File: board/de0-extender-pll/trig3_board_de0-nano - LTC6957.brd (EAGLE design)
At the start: 160 x 75 mm, 94 parts, among them IC1 FT230XQ, J12 4p-2.54, J13 BU-SMB-V, J17 2p-2.54, J23 2p-2.54, J24 2p-2.54, J32 2p-2.54, J34 2p-2.54, J38 2p-2.54, J42 2p-2.54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

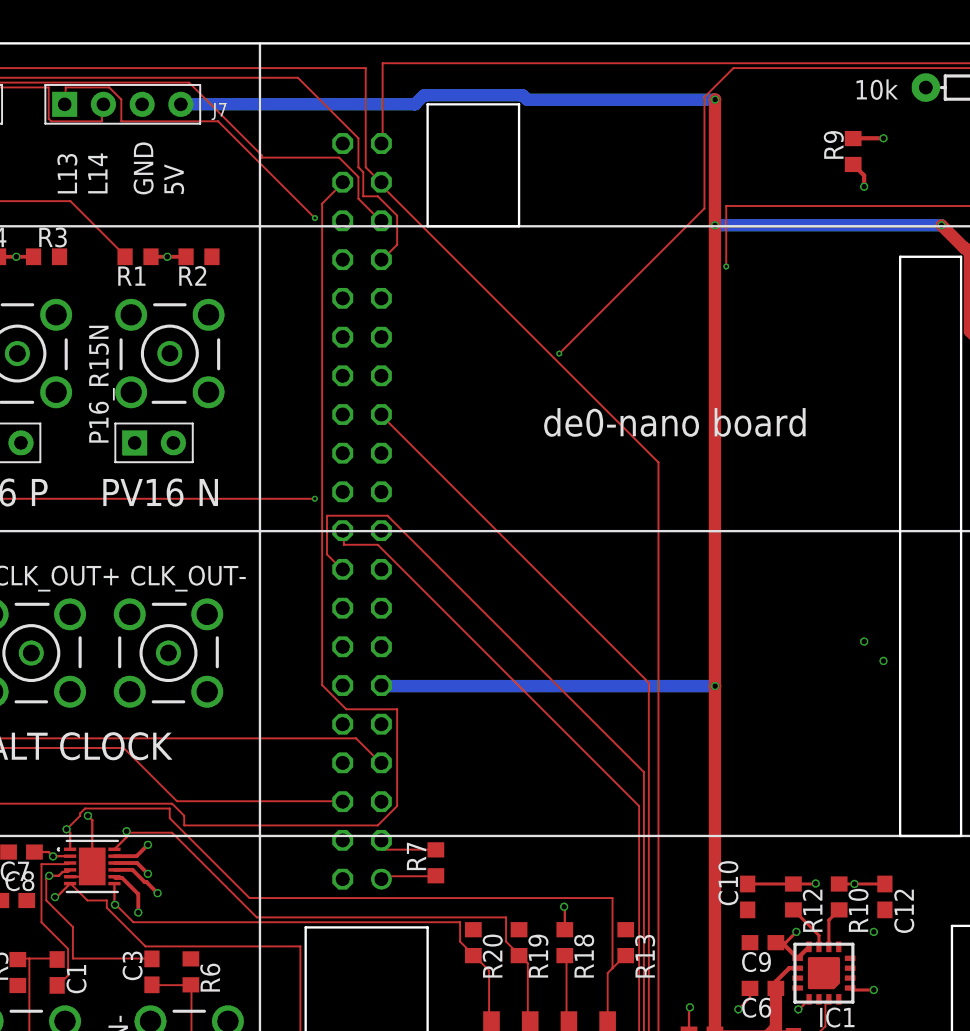
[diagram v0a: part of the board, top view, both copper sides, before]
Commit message: Update trig3_board_de0-nano - LTC6957.brd
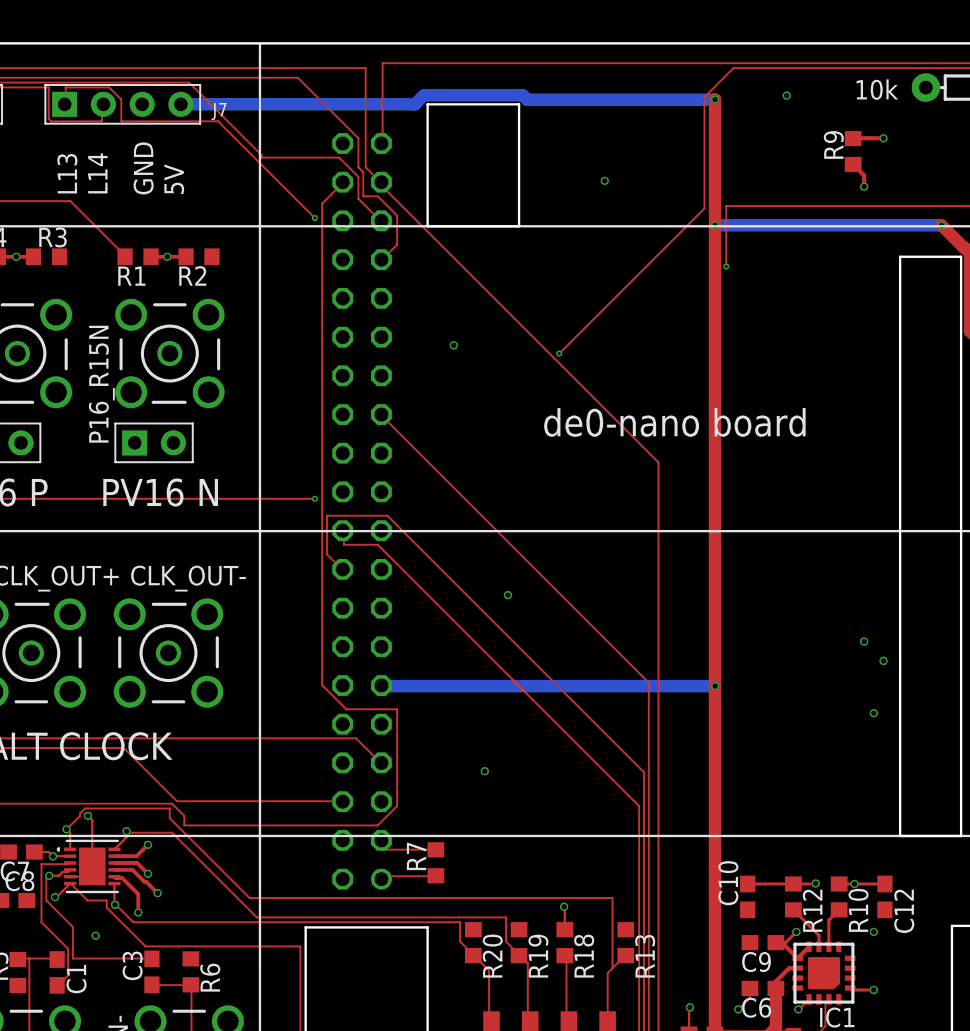
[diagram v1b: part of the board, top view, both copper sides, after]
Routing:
- net GND: vias 9 -> 10
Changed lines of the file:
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@@
 <wire x1="29.15" y1="47.692" x2="29.21" y2="47.752" width="0.1524" layer="1"/>
 <via x="29.21" y="47.752" extent="1-16" drill="0.35"/>
+<via x="23.622" y="101.981" extent="1-16" drill="0.35"/>
 </signal>
 <signal name="5V" class="1">
@@
 <wire x1="14.9225" y1="51.27625" x2="15" y2="51.15" width="0.127" layer="1"/>
 </signal>
+<signal name="GND1" airwireshidden="yes">
+<via x="13.716" y="91.186" extent="1-16" drill="0.35"/>
+</signal>
+<signal name="GND2" airwireshidden="yes">
+<via x="35.56" y="107.569" extent="1-16" drill="0.35"/>
+</signal>
+<signal name="GND3" airwireshidden="yes">
+<via x="17.272" y="74.803" extent="1-16" drill="0.35"/>
+</signal>
+<signal name="GND4" airwireshidden="yes">
+<via x="15.748" y="63.246" extent="1-16" drill="0.35"/>
+</signal>
+<signal name="GND6" airwireshidden="yes">
+<via x="41.275" y="67.056" extent="1-16" drill="0.35"/>
+</signal>
+<signal name="GND9" airwireshidden="yes">
+<via x="-9.779" y="52.451" extent="1-16" drill="0.35"/>
+</signal>
 </signals>

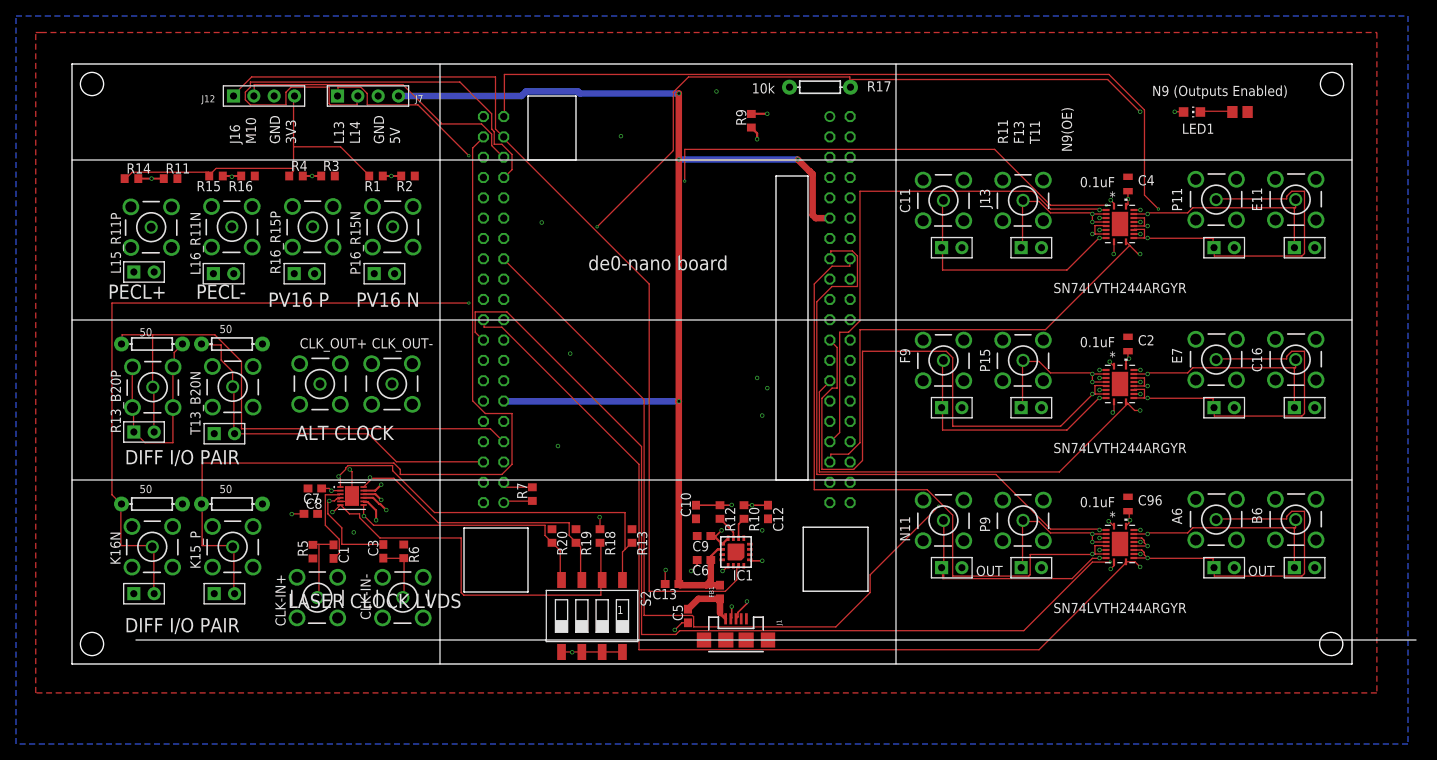
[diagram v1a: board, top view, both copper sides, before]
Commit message: fixed auto-router top layer nonsense
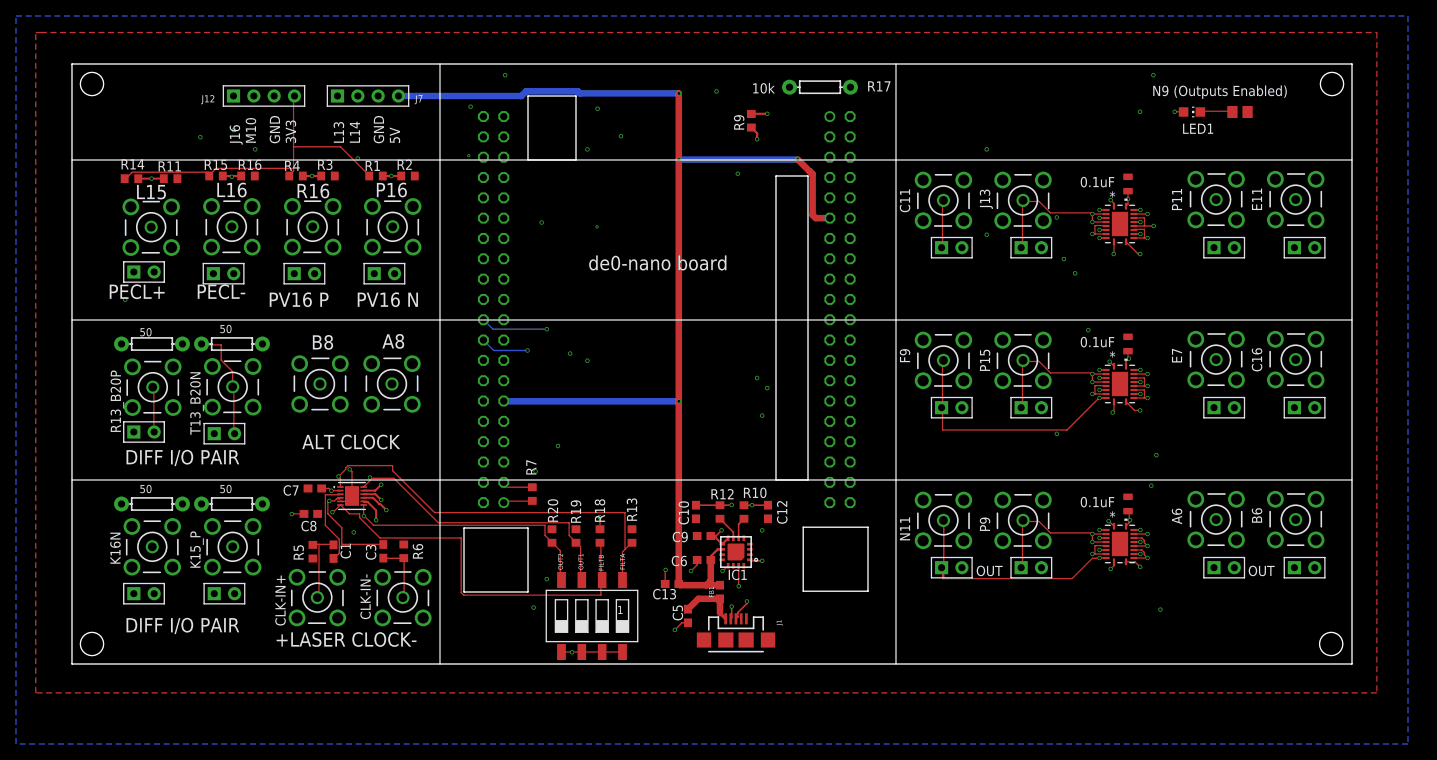
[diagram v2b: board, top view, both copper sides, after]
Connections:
- net N$15 renamed FILTA
- net N$16 renamed FILTB
- net N$17 renamed SD1
- net N$18 renamed SD2
- removed net N$1: J17.1, R13_B20P.2, R13_B20P.3, R13_B20P.4, R13_B20P.5, R161.P$1
- net GND: now also J17.1, R13_B20P.2, R13_B20P.3, R13_B20P.4, R13_B20P.5, R161.P$1
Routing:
- net GPIO_126_L14: track 63.7 -> 27.0 mm, vias 0 -> 1
- net GPIO_018_E7: track 80.5 -> 45.5 mm, vias 1 -> 2
- net N$1: track 26.5 -> 0.00 mm
- net OUT30: track 45.5 -> 19.1 mm
- net OUT38: track 45.5 -> 19.2 mm
- net OUT22: track 45.4 -> 19.0 mm
- net GPIO_110_P11: track 100.1 -> 115.0 mm, vias 3 -> 5
- net GPIO_14_R13: track 71.6 -> 57.9 mm
- net GPIO_022_F9: track 59.2 -> 45.6 mm
- net GPIO_011_A6: track 82.6 -> 69.4 mm, vias 1 -> 2
- net GPIO_131_K15: track 106.1 -> 95.0 mm, vias 0 -> 1
- net GPIO_120_P15: track 134.0 -> 123.0 mm, vias 2 -> 3
- net GPIO_028_C11: track 63.3 -> 72.9 mm, vias 2 -> 3
- net GPIO_010_B6: track 77.0 -> 67.7 mm, vias 2 -> 3
- net GPIO_130_J16: track 119.5 -> 123.8 mm, vias 0 -> 3
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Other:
- board text added: "+LASER CLOCK-"
- board text added: "A8"
- board text added: "B8"
- board text added: "FILTA"
- board text added: "FILTB"
- board text added: "L15"
- board text added: "L16"
- board text added: "OUT1"
- board text added: "OUT2"
- board text added: "P16"
- board text added: "R16"
- board text removed: "F13"
- board text removed: "LASER CLOCK LVDS"
- board text removed: "N9(OE)"
- board text removed: "R11"
- board text removed: "T11"

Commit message: removed wire stubs, tried to fix package rotation
rotated footprints in library but change did not propagate to pcb
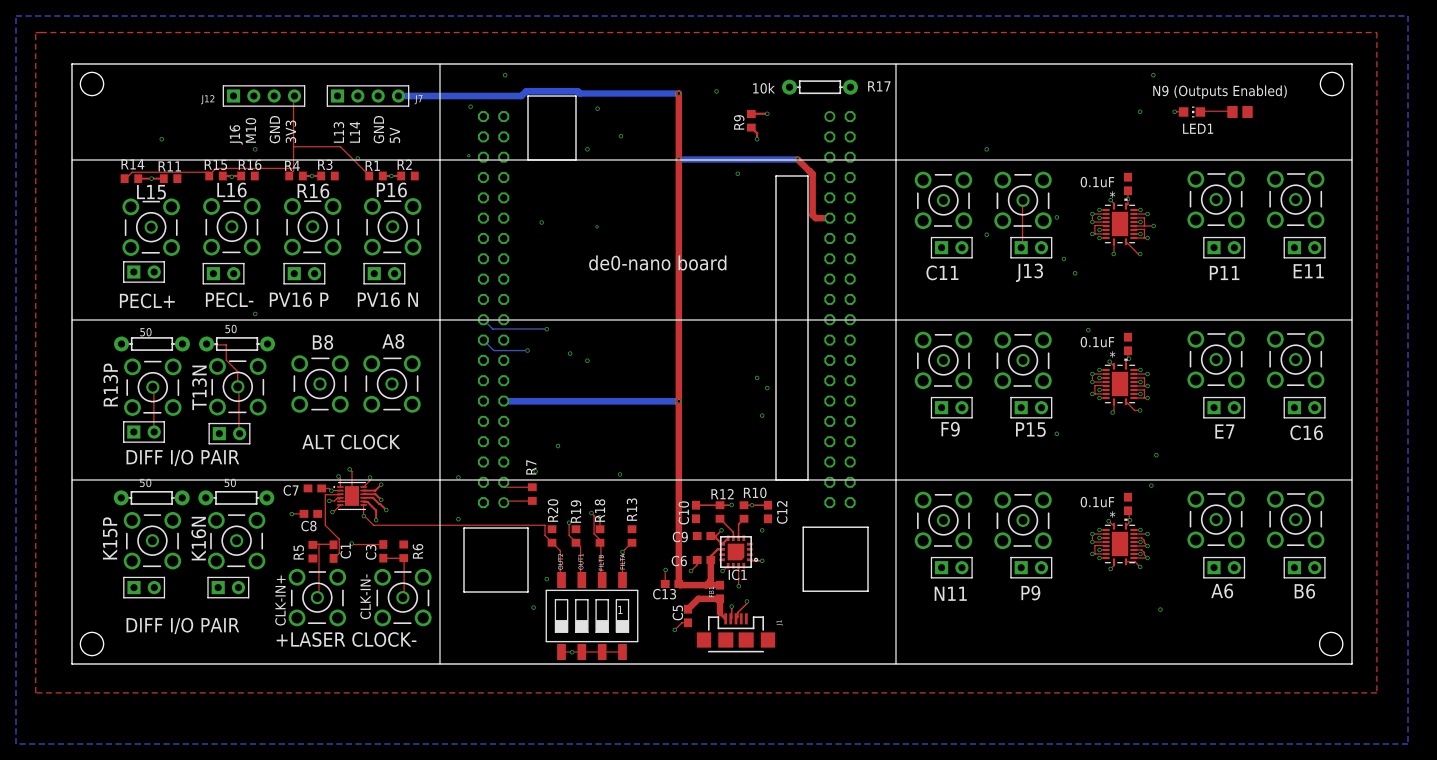
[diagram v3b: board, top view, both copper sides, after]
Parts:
- removed K15_P, T13_B20N: BU-SMB-V, con-coax:BU-SMB-V
- added K15P, T13N: BU-SMB-V, con-coax:BU-SMB-V
- C2, C4, C96: device SparkFun-Capacitors:0805 -> rcl:C0603
- R11, R16, R2, R3: value 83 -> 82
- moved K16N 10.6 mm to (-24.4, 51.4)
- moved R22 10.6 mm to (-24.5, 56.8)
- moved J23 10.6 mm to (-25.5, 45.6)
- moved J24 10.1 mm to (-36.0, 45.6)
- moved R23 10.1 mm to (-35.0, 56.8)
- moved J38 0.64 mm to (-25.3, 64.8)
- moved R32 0.64 mm to (-24.4, 76.0)
- renumbered R13_B20P to R13P
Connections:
- net GND: now also K15P.2, K15P.3, K15P.4, K15P.5, T13N.2, T13N.3, T13N.4, T13N.5; no longer K15_P.2, K15_P.3, K15_P.4, K15_P.5, T13_B20N.2, T13_B20N.3, T13_B20N.4, T13_B20N.5
- net GPIO_131_K15: now also K15P.1; no longer K15_P.1
- net GPIO_13_T13: now also T13N.1; no longer T13_B20N.1
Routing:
- net GPIO_117_K16: track 84.4 -> 71.8 mm
- net GPIO_131_K15: track 95.0 -> 103.2 mm
- net FILTB: track 49.7 -> 42.9 mm, vias 1 -> 2
- net OUT32: track 32.9 -> 29.2 mm
- net OUT24: track 32.1 -> 29.0 mm
- net SD1: track 36.7 -> 39.7 mm, vias 1 -> 4
- net FILTA: track 50.5 -> 52.4 mm, vias 1 -> 3
- net GPIO_13_T13: track 46.9 -> 46.3 mm
- net N$5: track 13.0 -> 12.3 mm, vias 1 -> 2
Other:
- board text removed: "OUT"

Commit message: rotated footprints and cosmetic updates to board
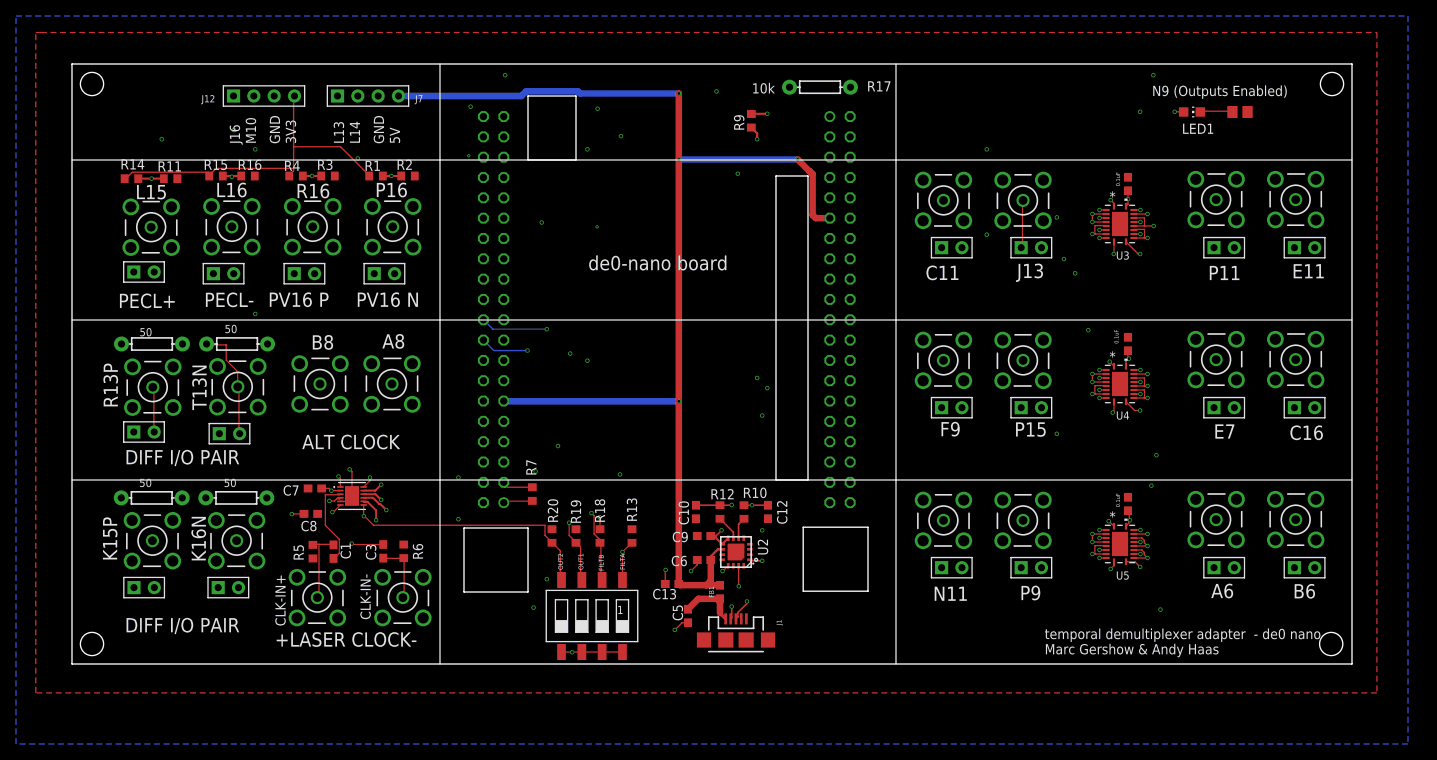
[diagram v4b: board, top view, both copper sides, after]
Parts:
- removed IC1: FT230XQ, ftdichip:QFN16
- added U2: FT230XQ, ftdichip-rotate-footprint-jlcpcb:QFN16
- turned U1 to 270 degrees
- turned U3 to 270 degrees
- turned U4 to 270 degrees
- turned U5 to 270 degrees
- renumbered VSLUE5 to U5, VSLUE7 to U4, VSLUE9 to U3
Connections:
- net 5V: now also U2.10; no longer IC1.10
- net GND: now also U2.13, U2.2, U2.3; no longer IC1.13, IC1.2, IC1.3
- net GPIO_130_J16: now also U2.15; no longer IC1.15
- net N$12: now also U2.6; no longer IC1.6
- net N$13: now also U2.7; no longer IC1.7
- net N$14: now also U2.1, U2.8, U2.9; no longer IC1.1, IC1.8, IC1.9
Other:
- board text added: "26 pin connector (not connected) here"
- board text added: "solder de0-nano this side usb connector up leds and dip switches should be visible through respective cutouts"
- board text added: "temporal demultiplexer adapter - de0 nano Marc Gershow & Andy Haas"
- board text added: "temporal demultiplexer adapter; adapted by Marc Gershow from Andy Hass's trig3_board_de0_nano"

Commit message: ready for ordering
will probably need to do one last check
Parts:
- J1: value (none) -> USB micro-b
- LED1: device led:CHIP-LED0805 -> led:SML0805
- turned LED1 to 180 degrees
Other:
- board text added: "K"

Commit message: fixed usb connection error; changed connector; change dip switch part
added sd1, sd2, filta, filtb to gpio pins also
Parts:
- J1: value USB micro-b -> 10118192-0002LF; device SparkFun-Connectors:USB-MICROB -> 10118192-0002LF:AMPHENOL_10118192-0002LF
- moved C12 12.6 mm to (39.5, 42.7)
- moved R12 11.7 mm to (35.2, 43.3), turned to 90 degrees
- moved C10 11.7 mm to (32.9, 43.3), turned to 270 degrees
- moved R10 10.8 mm to (37.3, 44.3), turned to 90 degrees
- moved C6 8.60 mm to (42.2, 51.6), turned to 0 degrees
- moved C9 8.54 mm to (42.1, 49.2), turned to 0 degrees
- moved FB1 5.62 mm to (30.7, 43.2)
- moved C5 3.39 mm to (28.8, 43.2), turned to 270 degrees
- moved J1 2.46 mm to (35.8, 40.1), turned to 0 degrees
- moved U2 0.37 mm to (37.7, 50.2), turned to 270 degrees
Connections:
- removed net FILTA: R13.2, S2.1, U1.1
- removed net FILTB: R18.2, S2.2, U1.6
- removed net SD1: R19.2, S2.3, U1.12
- removed net SD2: R20.2, S2.4, U1.7
- net GND: now also J1.5, J1.S1, J1.S2, J1.S3, J1.S4, J1.S5, J1.S6; no longer J1.GND, U2.2
- net GPIO_10_F13: now also R20.2, S2.4, U1.7
- net GPIO_11_T15: now also R19.2, S2.3, U1.12
- net GPIO_128_M10: now also U2.2
- net GPIO_12_T14: now also R13.2, S2.1, U1.1
- net GPIO_15_T12: now also R18.2, S2.2, U1.6
- net N$11: now also J1.2; no longer J1.D-
- net N$6: now also J1.1; no longer J1.VBUS
- net N$7: now also J1.3; no longer J1.D+
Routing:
- net GPIO_128_M10: track 38.2 -> 113.1 mm, vias 1 -> 3
- net GPIO_12_T14: track 0.00 -> 54.0 mm, vias 0 -> 3
- net FILTA: track 52.4 -> 0.00 mm, vias 3 -> 0
- net GPIO_15_T12: track 0.00 -> 52.3 mm, vias 0 -> 3
- net GPIO_11_T15: track 0.00 -> 43.1 mm, vias 0 -> 4
- net FILTB: track 42.9 -> 0.00 mm, vias 2 -> 0
- net SD1: track 39.7 -> 0.00 mm, vias 4 -> 0
- net GPIO_10_F13: track 0.00 -> 35.1 mm, vias 0 -> 1
- net SD2: track 32.3 -> 0.00 mm, vias 1 -> 0
- net N$11: track 18.8 -> 4.68 mm, vias 2 -> 0
- net N$7: track 18.0 -> 6.12 mm, vias 2 -> 0
- net GPIO_130_J16: track 123.8 -> 112.7 mm
- net N$6: track 7.33 -> 0.00 mm
- net 5V: track 154.4 -> 160.3 mm, vias 4 -> 6
- net N$13: track 3.12 -> 7.08 mm
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- added copper zone on layer 1, net N$6
